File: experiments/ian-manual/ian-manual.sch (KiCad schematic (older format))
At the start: 12 parts, among them U1 74HC393, U2 7555, U3 74HC04, U4 74HC21, U5 74HC15, U6 74HC32

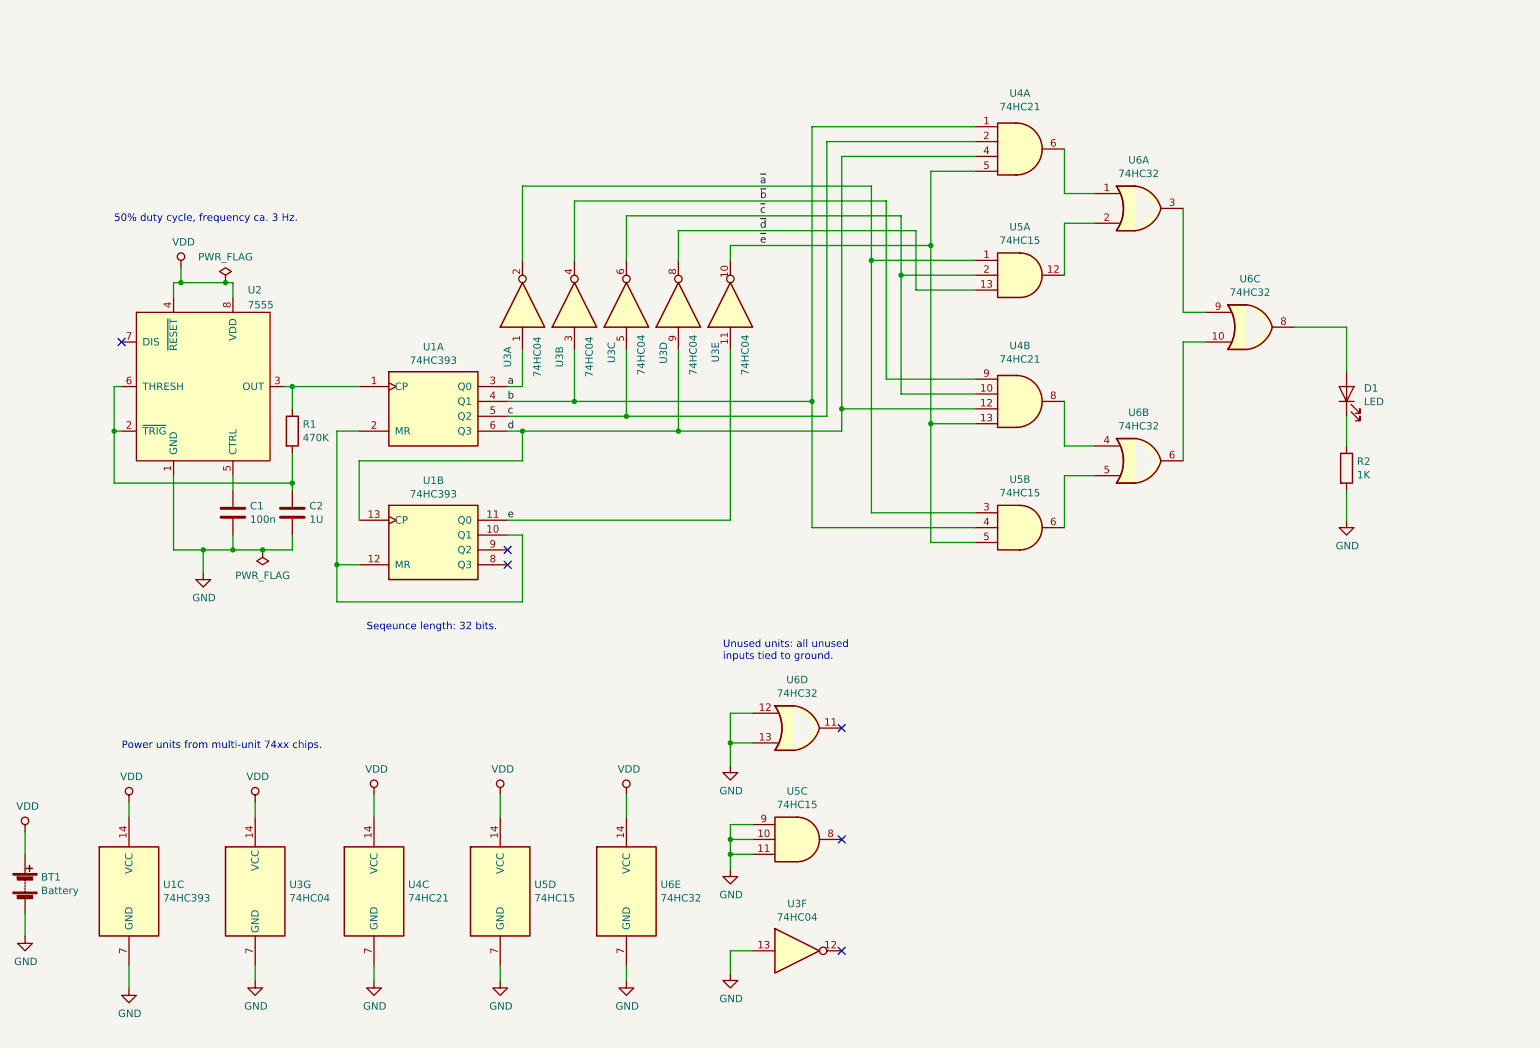
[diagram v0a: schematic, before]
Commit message: Tidying; templates for web app
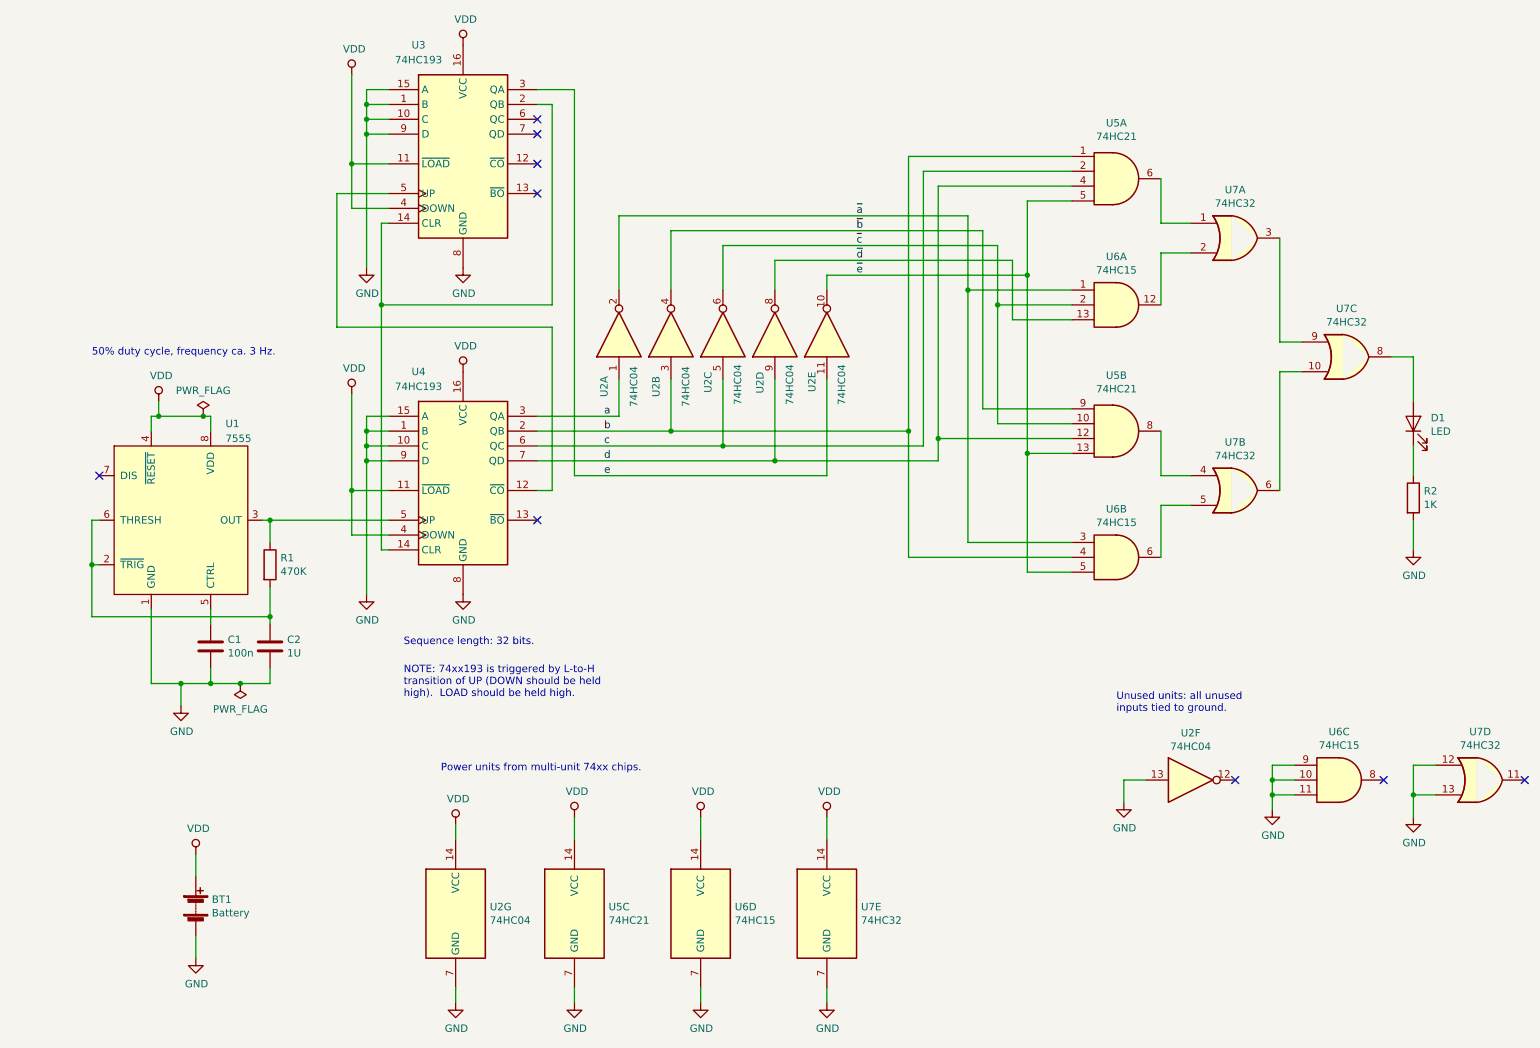
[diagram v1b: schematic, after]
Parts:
- removed U1: 74HC393, symbol morse-blinky:74HC393
- added U3, U4: 74HC193, Package_SO:SOIC-16_3.9x9.9mm_P1.27mm, symbol morse-blinky:74HC193
- BT1: footprint (none) -> morse-blinkies:BatteryHolder_LINK_BAT-HLD-001-SMT
- C1, C2: footprint (none) -> Capacitor_SMD:C_0805_2012Metric_Pad1.15x1.40mm_HandSolder
- D1: footprint (none) -> LED_SMD:LED_0805_2012Metric_Pad1.15x1.40mm_HandSolder
- R1, R2: footprint (none) -> Resistor_SMD:R_0805_2012Metric_Pad1.15x1.40mm_HandSolder
- U1: renamed from U2; footprint (none) -> Package_SO:SOIC-8_3.9x4.9mm_P1.27mm
- U2: renamed from U3; footprint (none) -> Package_SO:SOIC-14_3.9x8.7mm_P1.27mm
- U5: renamed from U4; footprint (none) -> Package_SO:SOIC-14_3.9x8.7mm_P1.27mm
- U6: renamed from U5; footprint (none) -> Package_SO:SOIC-14_3.9x8.7mm_P1.27mm
- U7: renamed from U6; footprint (none) -> Package_SO:SOIC-14_3.9x8.7mm_P1.27mm
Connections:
- net GND: now also U3.1 (B), U3.10 (C), U3.15 (A), U3.8 (GND), U3.9 (D), U4.1 (B), U4.10 (C), U4.15 (A), U4.8 (GND), U4.9 (D)
- net VDD: now also U3.11 (~LOAD), U3.16 (VCC), U3.4 (DOWN), U4.11 (~LOAD), U4.16 (VCC), U4.4 (DOWN)
- net a: now also U4.3 (QA)
- net b: now also U4.2 (QB)
- net c: now also U4.6 (QC)
- net d: now also U4.7 (QD)
- net e: now also U3.3 (QA)
- net at R1.1, U1.3 (OUT): now also U4.5 (UP)
- new net: U3.14 (CLR), U3.2 (QB), U4.14 (CLR)
- new net: U3.5 (UP), U4.12 (~CO)
- no-connect marks 6 -> 9
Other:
- note added: "NOTE: 74xx193 is triggered by L-to-H\ntransition of UP (DOWN should be held\nhigh). LOAD should be held high."
- note added: "Sequence length: 32 bits."
- note removed: "Seqeunce length: 32 bits."
- moved on the sheet: BT1, C1, C2, D1, R1, R2, U1, U2A, U2B, U2C, U2D, U2E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
